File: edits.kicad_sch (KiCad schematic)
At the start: 9 parts, among them J1301 DIN-5_180degree, U1301 EL817, U1302 EL817

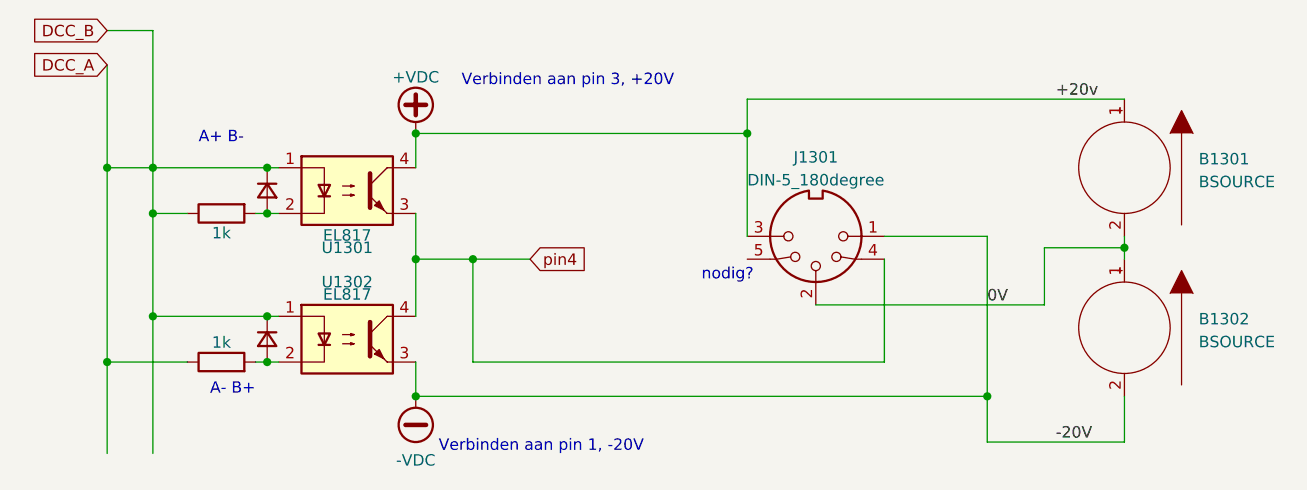
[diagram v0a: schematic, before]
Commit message: added hierarchial labels to some schematics
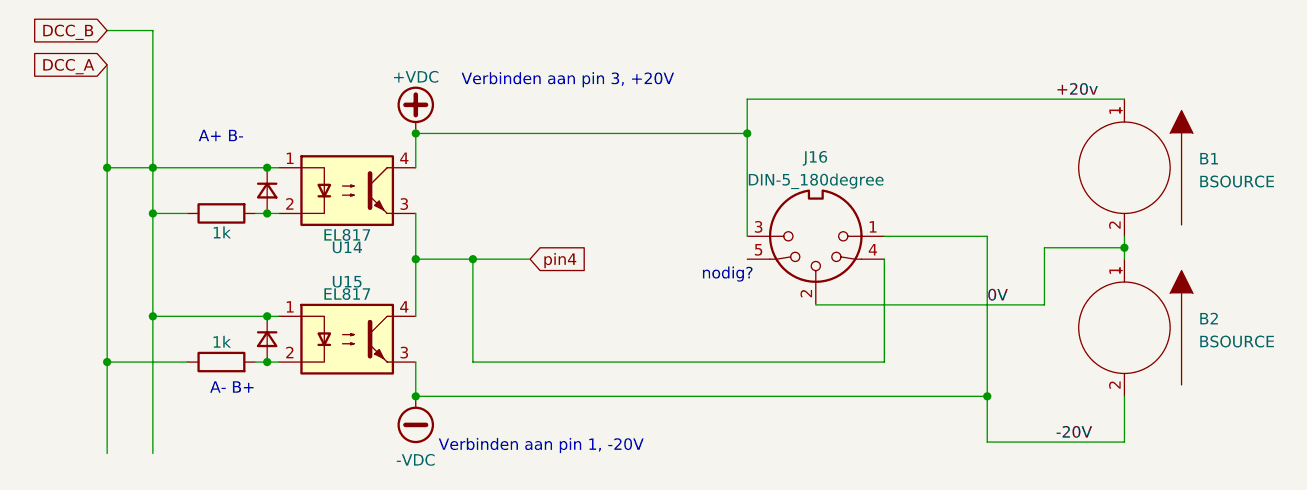
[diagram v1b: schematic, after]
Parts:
- renumbered B1301 to B1, B1302 to B2, D1301 to D26, D1302 to D27, J1301 to J16, R1301 to R37, R1302 to R38, U1301 to U14, U1302 to U15

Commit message: moved some schematic scheets to their own folders and routed a board with it. This allow for re-use of PCB parts.
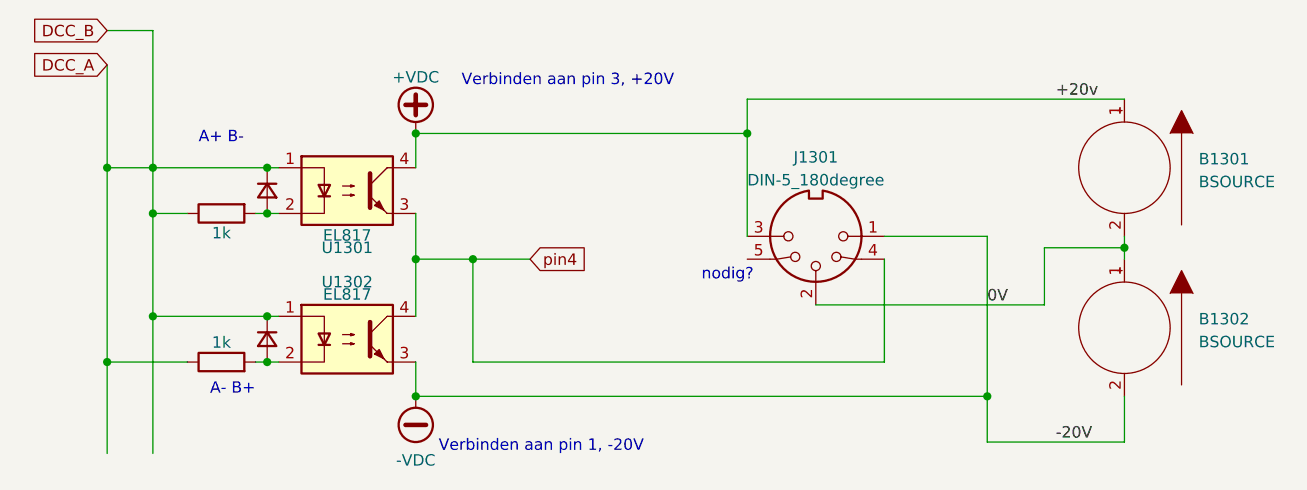
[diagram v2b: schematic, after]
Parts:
- renumbered B1 to B1301, B2 to B1302, D26 to D1301, D27 to D1302, J16 to J1301, R37 to R1301, R38 to R1302, U14 to U1301, U15 to U1302
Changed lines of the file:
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@@
   (symbol (lib_id "Device:D_Small") (at 138.43 82.55 90) (mirror x) (unit 1)
     (in_bom yes) (on_board yes) (dnp no) (fields_autoplaced)
-    (property "Reference" "D26" (at 140.208 83.3847 90)
+    (property "Reference" "D1301" (at 140.208 83.3847 90)
       (effects (font (size 1.27 1.27)) (justify right) hide)
     )
@@
       (project "general_schematics"
         (path "/e777d9ec-d073-4229-a9e6-2cf85636e407/aabb776b-8585-481a-9ba8-7761b2bc46d6"
-          (reference "D26") (unit 1)
+          (reference "D1301") (unit 1)
         )
       )
@@
   (symbol (lib_id "Connector:DIN-5_180degree") (at 199.39 87.63 180) (unit 1)
     (in_bom yes) (on_board yes) (dnp no) (fields_autoplaced)
-    (property "Reference" "J16" (at 199.3899 78.8502 0)
+    (property "Reference" "J1301" (at 199.3899 78.8502 0)
       (effects (font (size 1.27 1.27)))
     )
@@
       (project "general_schematics"
         (path "/e777d9ec-d073-4229-a9e6-2cf85636e407/aabb776b-8585-481a-9ba8-7761b2bc46d6"
-          (reference "J16") (unit 1)
+          (reference "J1301") (unit 1)
         )
       )
@@
   (symbol (lib_id "pspice:BSOURCE") (at 233.68 80.01 0) (mirror y) (unit 1)
     (in_bom yes) (on_board yes) (dnp no) (fields_autoplaced)
-    (property "Reference" "B1" (at 241.935 79.0483 0)
+    (property "Reference" "B1301" (at 241.935 79.0483 0)
       (effects (font (size 1.27 1.27)) (justify right))
     )
@@
       (project "general_schematics"
         (path "/e777d9ec-d073-4229-a9e6-2cf85636e407/aabb776b-8585-481a-9ba8-7761b2bc46d6"
-          (reference "B1") (unit 1)
+          (reference "B1301") (unit 1)
         )
       )
@@
   (symbol (lib_id "Isolator:EL817") (at 147.32 82.55 0) (unit 1)
     (in_bom yes) (on_board yes) (dnp no)
-    (property "Reference" "U14" (at 147.32 88.9 0)
+    (property "Reference" "U1301" (at 147.32 88.9 0)
       (effects (font (size 1.27 1.27)))
     )
@@
       (project "general_schematics"
         (path "/e777d9ec-d073-4229-a9e6-2cf85636e407/aabb776b-8585-481a-9ba8-7761b2bc46d6"
-          (reference "U14") (unit 1)
+          (reference "U1301") (unit 1)
         )
       )
@@
   (symbol (lib_id "Isolator:EL817") (at 147.32 99.06 0) (unit 1)
     (in_bom yes) (on_board yes) (dnp no)
-    (property "Reference" "U15" (at 147.32 92.71 0)
+    (property "Reference" "U1302" (at 147.32 92.71 0)
       (effects (font (size 1.27 1.27)))
     )
@@
       (project "general_schematics"
         (path "/e777d9ec-d073-4229-a9e6-2cf85636e407/aabb776b-8585-481a-9ba8-7761b2bc46d6"
-          (reference "U15") (unit 1)
+          (reference "U1302") (unit 1)
         )
       )
@@
   (symbol (lib_id "Device:D_Small") (at 138.43 99.06 270) (unit 1)
     (in_bom yes) (on_board yes) (dnp no) (fields_autoplaced)
-    (property "Reference" "D27" (at 136.652 99.8947 90)
+    (property "Reference" "D1302" (at 136.652 99.8947 90)
       (effects (font (size 1.27 1.27)) (justify right) hide)
     )
@@
       (project "general_schematics"
         (path "/e777d9ec-d073-4229-a9e6-2cf85636e407/aabb776b-8585-481a-9ba8-7761b2bc46d6"
-          (reference "D27") (unit 1)
+          (reference "D1302") (unit 1)
         )
       )
@@
   (symbol (lib_id "Device:R") (at 133.35 85.09 90) (mirror x) (unit 1)
     (in_bom yes) (on_board yes) (dnp no) (fields_autoplaced)
-    (property "Reference" "R37" (at 133.35 89.8058 90)
+    (property "Reference" "R1301" (at 133.35 89.8058 90)
       (effects (font (size 1.27 1.27)) hide)
     )
@@
       (project "general_schematics"
         (path "/e777d9ec-d073-4229-a9e6-2cf85636e407/aabb776b-8585-481a-9ba8-7761b2bc46d6"
-          (reference "R37") (unit 1)
+          (reference "R1301") (unit 1)
         )
       )
@@
   (symbol (lib_id "power:-VDC") (at 154.94 105.41 180) (unit 1)
     (in_bom yes) (on_board yes) (dnp no) (fields_autoplaced)
-    (property "Reference" "#PWR052" (at 154.94 102.87 0)
+    (property "Reference" "#PWR0136" (at 154.94 102.87 0)
       (effects (font (size 1.27 1.27)) hide)
     )
@@
       (project "general_schematics"
         (path "/e777d9ec-d073-4229-a9e6-2cf85636e407/aabb776b-8585-481a-9ba8-7761b2bc46d6"
-          (reference "#PWR052") (unit 1)
+          (reference "#PWR0136") (unit 1)
         )
       )
@@
   (symbol (lib_id "pspice:BSOURCE") (at 233.68 97.79 0) (mirror y) (unit 1)
     (in_bom yes) (on_board yes) (dnp no) (fields_autoplaced)
-    (property "Reference" "B2" (at 241.935 96.8283 0)
+    (property "Reference" "B1302" (at 241.935 96.8283 0)
       (effects (font (size 1.27 1.27)) (justify right))
     )
@@
       (project "general_schematics"
         (path "/e777d9ec-d073-4229-a9e6-2cf85636e407/aabb776b-8585-481a-9ba8-7761b2bc46d6"
-          (reference "B2") (unit 1)
+          (reference "B1302") (unit 1)
         )
       )
@@
   (symbol (lib_id "Device:R") (at 133.35 101.6 90) (unit 1)
     (in_bom yes) (on_board yes) (dnp no) (fields_autoplaced)
-    (property "Reference" "R38" (at 133.35 96.8842 90)
+    (property "Reference" "R1302" (at 133.35 96.8842 90)
       (effects (font (size 1.27 1.27)) hide)
     )
@@
       (project "general_schematics"
         (path "/e777d9ec-d073-4229-a9e6-2cf85636e407/aabb776b-8585-481a-9ba8-7761b2bc46d6"
-          (reference "R38") (unit 1)
+          (reference "R1302") (unit 1)
         )
       )
@@
   (symbol (lib_id "power:+VDC") (at 154.94 76.2 0) (unit 1)
     (in_bom yes) (on_board yes) (dnp no) (fields_autoplaced)
-    (property "Reference" "#PWR051" (at 154.94 78.74 0)
+    (property "Reference" "#PWR0135" (at 154.94 78.74 0)
       (effects (font (size 1.27 1.27)) hide)
     )
@@
       (project "general_schematics"
         (path "/e777d9ec-d073-4229-a9e6-2cf85636e407/aabb776b-8585-481a-9ba8-7761b2bc46d6"
-          (reference "#PWR051") (unit 1)
-        )
-      )
+          (reference "#PWR0135") (unit 1)
+        )
+      )
